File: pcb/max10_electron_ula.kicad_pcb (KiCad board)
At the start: 4 copper layers, 50 x 50 mm, 20 parts

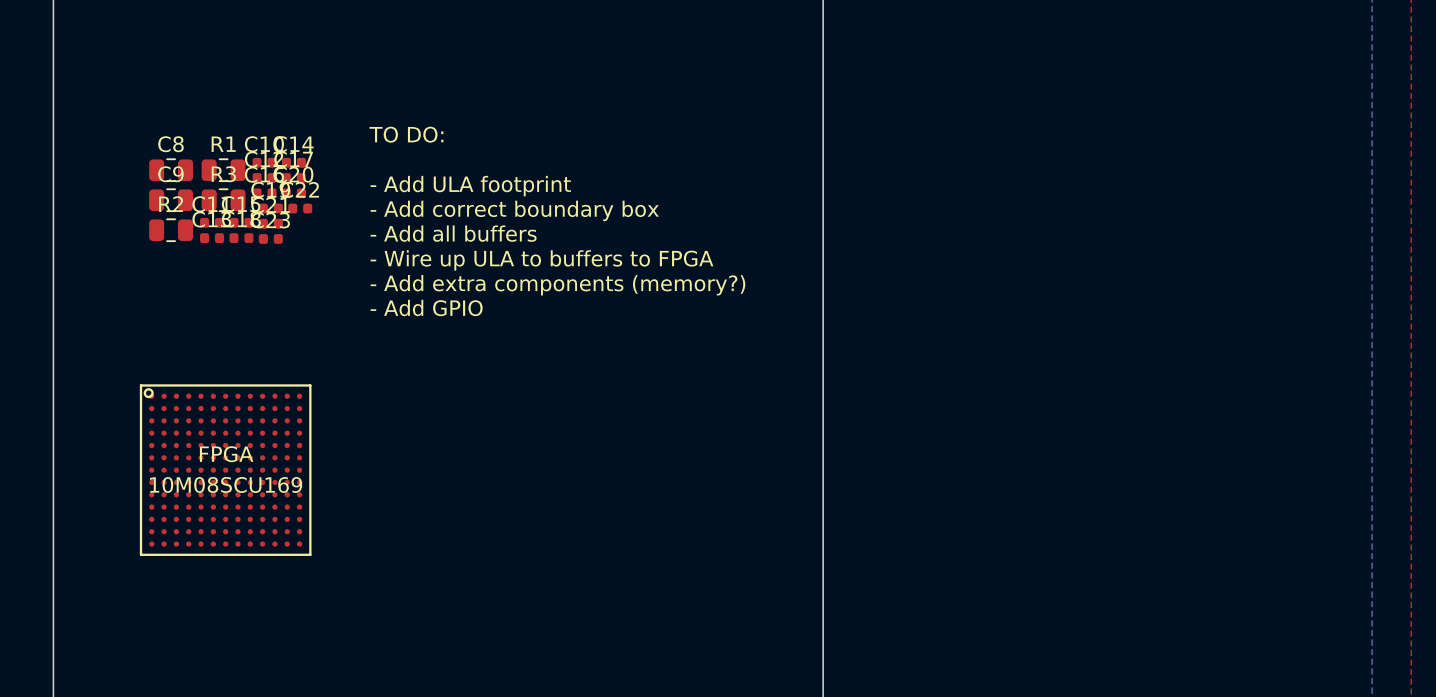
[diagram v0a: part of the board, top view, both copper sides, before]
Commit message: Added notes on ULA signals, with quotes from Stardot, and added ULA footprint
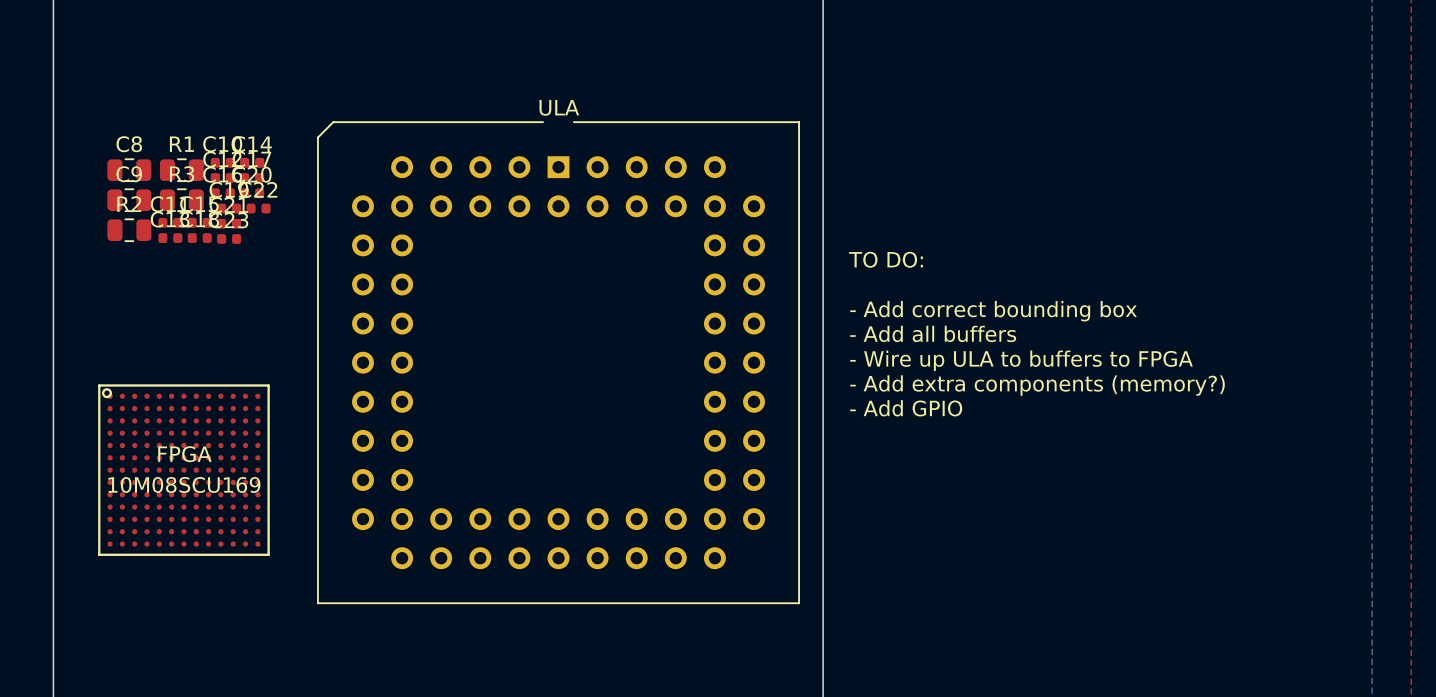
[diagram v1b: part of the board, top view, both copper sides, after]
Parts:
- added ULA: ULA header, Package_LCC:PLCC-68_THT-Socket, F.Cu at (147.8, 57.6)
- moved C10 2.71 mm to (126.0, 57.3)
- moved C11 2.71 mm to (122.6, 61.2)
- moved C12 2.71 mm to (126.0, 58.3)
- moved C13 2.71 mm to (122.6, 62.2)
- moved C15 2.71 mm to (124.5, 61.2)
- moved C16 2.71 mm to (126.0, 59.3)
- moved C18 2.71 mm to (124.5, 62.2)
- moved C22 2.71 mm to (128.3, 60.2)
- moved R1 2.71 mm to (123.3, 57.8)
- moved R3 2.71 mm to (123.3, 59.7)
- moved C14 2.71 mm to (127.9, 57.3)
- moved C17 2.71 mm to (127.9, 58.3)
- moved C19 2.71 mm to (126.4, 60.2)
- moved C20 2.71 mm to (127.9, 59.3)
- moved C21 2.71 mm to (126.4, 61.2)
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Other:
- board text added: "TO DO: - Add correct bounding box - Add all buffers - Wire up ULA to buffers to FPGA - Add extra components (memory?) - Add GPIO"
- board text removed: "TO DO: - Add ULA footprint - Add correct boundary box - Add all buffers - Wire up ULA to buffers to FPGA - Add extra components (memory?) - Add GPIO"

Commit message: Added 8MB flash chip
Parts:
- added FC0: 100n, Capacitor_SMD:C_0805_2012Metric_Pad1.15x1.40mm_HandSolder, F.Cu at (129.3, 85.3)
- added FC1: 100n, Capacitor_SMD:C_0805_2012Metric_Pad1.15x1.40mm_HandSolder, F.Cu at (129.3, 87.2)
- added FC2: 100n, Capacitor_SMD:C_0805_2012Metric_Pad1.15x1.40mm_HandSolder, F.Cu at (129.3, 89.2)
- added FLASH: S29GL064S70DHI010, myelin-kicad:cypress_lae064_fbga, F.Cu at (122.8, 88.9)

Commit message: Added 3.3V regulator and capacitors
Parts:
- added C1: 10u, Capacitor_SMD:C_0805_2012Metric_Pad1.15x1.40mm_HandSolder, F.Cu at (151.2, 68.4)
- added C2: 1u, Capacitor_SMD:C_0805_2012Metric_Pad1.15x1.40mm_HandSolder, F.Cu at (151.2, 70.3)
- added C3: 1u, Capacitor_SMD:C_0805_2012Metric_Pad1.15x1.40mm_HandSolder, F.Cu at (151.2, 72.3)
- added REG: AP7365-33YG-XX, Package_TO_SOT_SMD:SOT-89-3, F.Cu at (146.0, 70.0)
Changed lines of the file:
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@@
     (tracks 0)
     (zones 0)
-    (modules 25)
-    (nets 141)
+    (modules 29)
+    (nets 142)
   )
   (page A4)
@@
   (net 139 flash_DQ4)
   (net 140 flash_DQ6)
+  (net 141 5V)
   (net_class Default "This is the default net class."
     (clearance 0.127)
@@
     (uvia_dia 0.8128)
     (uvia_drill 0.3302)
+    (add_net 5V)
     (add_net C1_1)
     (add_net C1_10)
@@
       (solder_mask_margin 0.075) (clearance 0.1639))
   )
+  (module Capacitor_SMD:C_0805_2012Metric_Pad1.15x1.40mm_HandSolder (layer F.Cu)
+    (at 151.155001 68.375001)
+    (descr "Capacitor SMD 0805 (2012 Metric), square (rectangular) end terminal, IPC_7351 nominal with elongated pad for handsoldering. (Body size source: https://docs.google.com/spreadsheets/d/1BsfQQcO9C6DZCsRaXUlFlo91Tg2WpOkGARC1WS5S8t0/edit?usp=sharing), generated with kicad-footprint-generator")
+    (tags "capacitor handsolder")
+    (attr smd)
+    (fp_text reference C1 (at 0 -1.65) (layer F.SilkS)
+      (effects (font (size 1 1) (thickness 0.15)))
+    )
+    (fp_text value 10u (at 0 1.65) (layer F.Fab)
+      (effects (font (size 1 1) (thickness 0.15)))
+    )
+    (fp_line (start -1 0.6) (end -1 -0.6) (layer F.Fab) (width 0.1))
+    (fp_line (start -1 -0.6) (end 1 -0.6) (layer F.Fab) (width 0.1))
+    (fp_line (start 1 -0.6) (end 1 0.6) (layer F.Fab) (width 0.1))
+    (fp_line (start 1 0.6) (end -1 0.6) (layer F.Fab) (width 0.1))
+    (fp_line (start -0.261252 -0.71) (end 0.261252 -0.71) (layer F.SilkS) (width 0.12))
+    (fp_line (start -0.261252 0.71) (end 0.261252 0.71) (layer F.SilkS) (width 0.12))
+    (fp_line (start -1.85 0.95) (end -1.85 -0.95) (layer F.CrtYd) (width 0.05))
+    (fp_line (start -1.85 -0.95) (end 1.85 -0.95) (layer F.CrtYd) (width 0.05))
+    (fp_line (start 1.85 -0.95) (end 1.85 0.95) (layer F.CrtYd) (width 0.05))
+    (fp_line (start 1.85 0.95) (end -1.85 0.95) (layer F.CrtYd) (width 0.05))
+    (fp_text user %R (at 0 0) (layer F.Fab)
+      (effects (font (size 0.5 0.5) (thickness 0.08)))
+    )
+    (pad 1 smd roundrect (at -1.025 0) (size 1.15 1.4) (layers F.Cu F.Paste F.Mask) (roundrect_rratio 0.217391)
+      (net 2 GND))
+    (pad 2 smd roundrect (at 1.025 0) (size 1.15 1.4) (layers F.Cu F.Paste F.Mask) (roundrect_rratio 0.217391)
+      (net 141 5V))
+    (model ${KISYS3DMOD}/Capacitor_SMD.3dshapes/C_0805_2012Metric.wrl
+      (at (xyz 0 0 0))
+      (scale (xyz 1 1 1))
+      (rotate (xyz 0 0 0))
+    )
+  )
+  (module Capacitor_SMD:C_0805_2012Metric_Pad1.15x1.40mm_HandSolder (layer F.Cu)
+    (at 151.155001 70.325001)
+    (descr "Capacitor SMD 0805 (2012 Metric), square (rectangular) end terminal, IPC_7351 nominal with elongated pad for handsoldering. (Body size source: https://docs.google.com/spreadsheets/d/1BsfQQcO9C6DZCsRaXUlFlo91Tg2WpOkGARC1WS5S8t0/edit?usp=sharing), generated with kicad-footprint-generator")
+    (tags "capacitor handsolder")
+    (attr smd)
+    (fp_text reference C2 (at 0 -1.65) (layer F.SilkS)
+      (effects (font (size 1 1) (thickness 0.15)))
+    )
+    (fp_text value 1u (at 0 1.65) (layer F.Fab)
+      (effects (font (size 1 1) (thickness 0.15)))
+    )
+    (fp_text user %R (at 0 0) (layer F.Fab)
+      (effects (font (size 0.5 0.5) (thickness 0.08)))
+    )
+    (fp_line (start 1.85 0.95) (end -1.85 0.95) (layer F.CrtYd) (width 0.05))
+    (fp_line (start 1.85 -0.95) (end 1.85 0.95) (layer F.CrtYd) (width 0.05))
+    (fp_line (start -1.85 -0.95) (end 1.85 -0.95) (layer F.CrtYd) (width 0.05))
+    (fp_line (start -1.85 0.95) (end -1.85 -0.95) (layer F.CrtYd) (width 0.05))
+    (fp_line (start -0.261252 0.71) (end 0.261252 0.71) (layer F.SilkS) (width 0.12))
+    (fp_line (start -0.261252 -0.71) (end 0.261252 -0.71) (layer F.SilkS) (width 0.12))
+    (fp_line (start 1 0.6) (end -1 0.6) (layer F.Fab) (width 0.1))
+    (fp_line (start 1 -0.6) (end 1 0.6) (layer F.Fab) (width 0.1))
+    (fp_line (start -1 -0.6) (end 1 -0.6) (layer F.Fab) (width 0.1))
+    (fp_line (start -1 0.6) (end -1 -0.6) (layer F.Fab) (width 0.1))
+    (pad 2 smd roundrect (at 1.025 0) (size 1.15 1.4) (layers F.Cu F.Paste F.Mask) (roundrect_rratio 0.217391)
+      (net 141 5V))
+    (pad 1 smd roundrect (at -1.025 0) (size 1.15 1.4) (layers F.Cu F.Paste F.Mask) (roundrect_rratio 0.217391)
+      (net 2 GND))
+    (model ${KISYS3DMOD}/Capacitor_SMD.3dshapes/C_0805_2012Metric.wrl
+      (at (xyz 0 0 0))
+      (scale (xyz 1 1 1))
+      (rotate (xyz 0 0 0))
+    )
+  )
+  (module Capacitor_SMD:C_0805_2012Metric_Pad1.15x1.40mm_HandSolder (layer F.Cu)
+    (at 151.155001 72.275001)
+    (descr "Capacitor SMD 0805 (2012 Metric), square (rectangular) end terminal, IPC_7351 nominal with elongated pad for handsoldering. (Body size source: https://docs.google.com/spreadsheets/d/1BsfQQcO9C6DZCsRaXUlFlo91Tg2WpOkGARC1WS5S8t0/edit?usp=sharing), generated with kicad-footprint-generator")
+    (tags "capacitor handsolder")
+    (attr smd)
+    (fp_text reference C3 (at 0 -1.65) (layer F.SilkS)
+      (effects (font (size 1 1) (thickness 0.15)))
+    )
+    (fp_text value 1u (at 0 1.65) (layer F.Fab)
+      (effects (font (size 1 1) (thickness 0.15)))
+    )
+    (fp_line (start -1 0.6) (end -1 -0.6) (layer F.Fab) (width 0.1))
+    (fp_line (start -1 -0.6) (end 1 -0.6) (layer F.Fab) (width 0.1))
+    (fp_line (start 1 -0.6) (end 1 0.6) (layer F.Fab) (width 0.1))
+    (fp_line (start 1 0.6) (end -1 0.6) (layer F.Fab) (width 0.1))
+    (fp_line (start -0.261252 -0.71) (end 0.261252 -0.71) (layer F.SilkS) (width 0.12))
+    (fp_line (start -0.261252 0.71) (end 0.261252 0.71) (layer F.SilkS) (width 0.12))
+    (fp_line (start -1.85 0.95) (end -1.85 -0.95) (layer F.CrtYd) (width 0.05))
+    (fp_line (start -1.85 -0.95) (end 1.85 -0.95) (layer F.CrtYd) (width 0.05))
+    (fp_line (start 1.85 -0.95) (end 1.85 0.95) (layer F.CrtYd) (width 0.05))
+    (fp_line (start 1.85 0.95) (end -1.85 0.95) (layer F.CrtYd) (width 0.05))
+    (fp_text user %R (at 0 0) (layer F.Fab)
+      (effects (font (size 0.5 0.5) (thickness 0.08)))
+    )
+    (pad 1 smd roundrect (at -1.025 0) (size 1.15 1.4) (layers F.Cu F.Paste F.Mask) (roundrect_rratio 0.217391)
+      (net 1 3V3))
+    (pad 2 smd roundrect (at 1.025 0) (size 1.15 1.4) (layers F.Cu F.Paste F.Mask) (roundrect_rratio 0.217391)
+      (net 2 GND))
+    (model ${KISYS3DMOD}/Capacitor_SMD.3dshapes/C_0805_2012Metric.wrl
+      (at (xyz 0 0 0))
+      (scale (xyz 1 1 1))
+      (rotate (xyz 0 0 0))
+    )
+  )
+  (module Package_TO_SOT_SMD:SOT-89-3 (layer F.Cu)
+    (at 146.025001 69.975001)
+    (descr SOT-89-3)
+    (tags SOT-89-3)
+    (attr smd)
+    (fp_text reference REG (at 0.45 -3.2) (layer F.SilkS)
+      (effects (font (size 1 1) (thickness 0.15)))
+    )
+    (fp_text value AP7365-33YG-XX (at 0.45 3.25) (layer F.Fab)
+      (effects (font (size 1 1) (thickness 0.15)))
+    )
+    (fp_text user %R (at 0.38 0 90) (layer F.Fab)
+      (effects (font (size 0.6 0.6) (thickness 0.09)))
+    )
+    (fp_line (start 1.78 1.2) (end 1.78 2.4) (layer F.SilkS) (width 0.12))
+    (fp_line (start 1.78 2.4) (end -0.92 2.4) (layer F.SilkS) (width 0.12))
+    (fp_line (start -2.22 -2.4) (end 1.78 -2.4) (layer F.SilkS) (width 0.12))
+    (fp_line (start 1.78 -2.4) (end 1.78 -1.2) (layer F.SilkS) (width 0.12))
+    (fp_line (start -0.92 -1.51) (end -0.13 -2.3) (layer F.Fab) (width 0.1))
+    (fp_line (start 1.68 -2.3) (end 1.68 2.3) (layer F.Fab) (width 0.1))
+    (fp_line (start 1.68 2.3) (end -0.92 2.3) (layer F.Fab) (width 0.1))
+    (fp_line (start -0.92 2.3) (end -0.92 -1.51) (layer F.Fab) (width 0.1))
+    (fp_line (start -0.13 -2.3) (end 1.68 -2.3) (layer F.Fab) (width 0.1))
+    (fp_line (start 3.23 -2.55) (end 3.23 2.55) (layer F.CrtYd) (width 0.05))
+    (fp_line (start 3.23 -2.55) (end -2.48 -2.55) (layer F.CrtYd) (width 0.05))
+    (fp_line (start -2.48 2.55) (end 3.23 2.55) (layer F.CrtYd) (width 0.05))
+    (fp_line (start -2.48 2.55) (end -2.48 -2.55) (layer F.CrtYd) (width 0.05))
+    (pad 2 smd trapezoid (at 2.667 0 270) (size 1.6 0.85) (rect_delta 0 0.6 ) (layers F.Cu F.Paste F.Mask)
+      (net 2 GND))
+    (pad 1 smd rect (at -1.48 -1.5 270) (size 1 1.5) (layers F.Cu F.Paste F.Mask)
+      (net 1 3V3))
+    (pad 2 smd rect (at -1.3335 0 270) (size 1 1.8) (layers F.Cu F.Paste F.Mask)
+      (net 2 GND))
+    (pad 3 smd rect (at -1.48 1.5 270) (size 1 1.5) (layers F.Cu F.Paste F.Mask)
+      (net 141 5V))
+    (pad 2 smd rect (at 1.3335 0 270) (size 2.2 1.84) (layers F.Cu F.Paste F.Mask)
+      (net 2 GND))
+    (pad 2 smd trapezoid (at -0.0762 0 90) (size 1.5 1) (rect_delta 0 0.7 ) (layers F.Cu F.Paste F.Mask)
+      (net 2 GND))
+    (model ${KISYS3DMOD}/Package_TO_SOT_SMD.3dshapes/SOT-89-3.wrl
+      (at (xyz 0 0 0))
+      (scale (xyz 1 1 1))
+      (rotate (xyz 0 0 0))
+    )
+  )
   (gr_line (start 115 95) (end 115 45) (layer Edge.Cuts) (width 0.1))

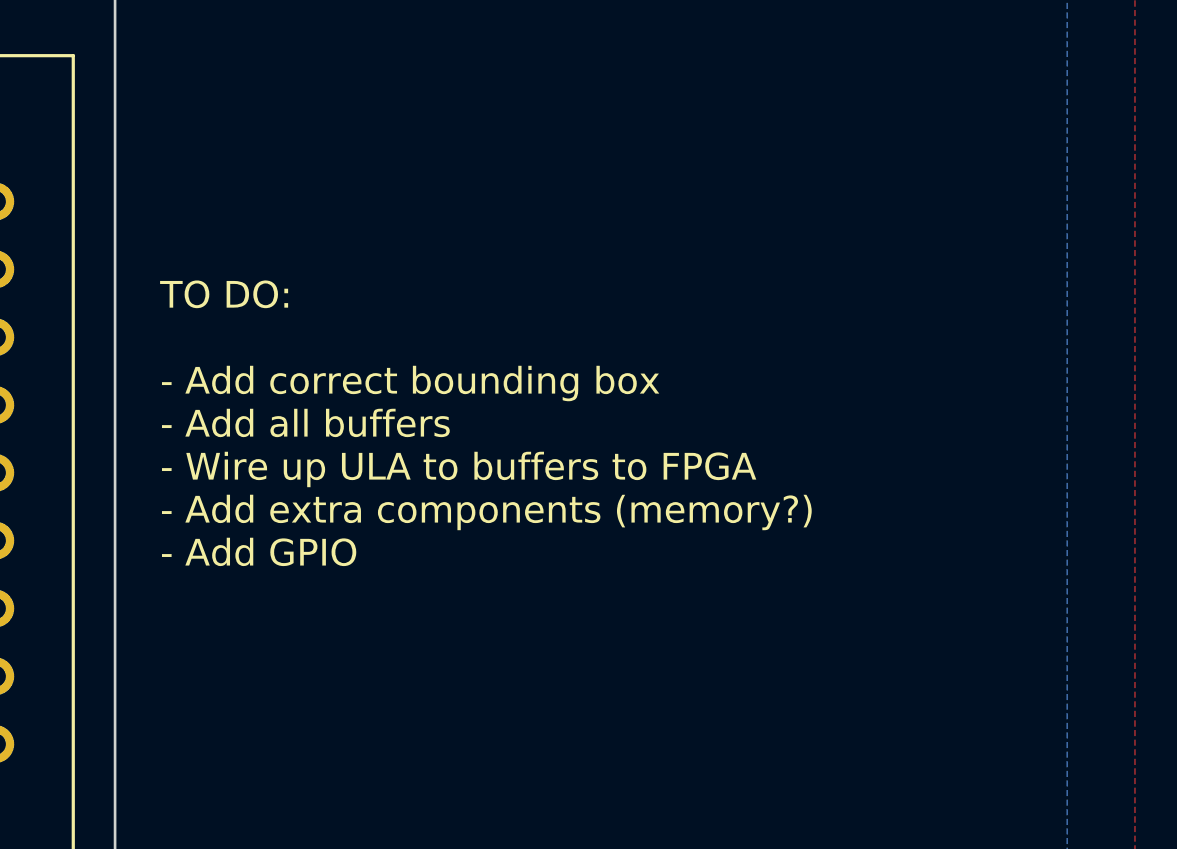
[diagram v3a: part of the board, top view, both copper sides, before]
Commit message: Added all ULA signals, and some RAM notes
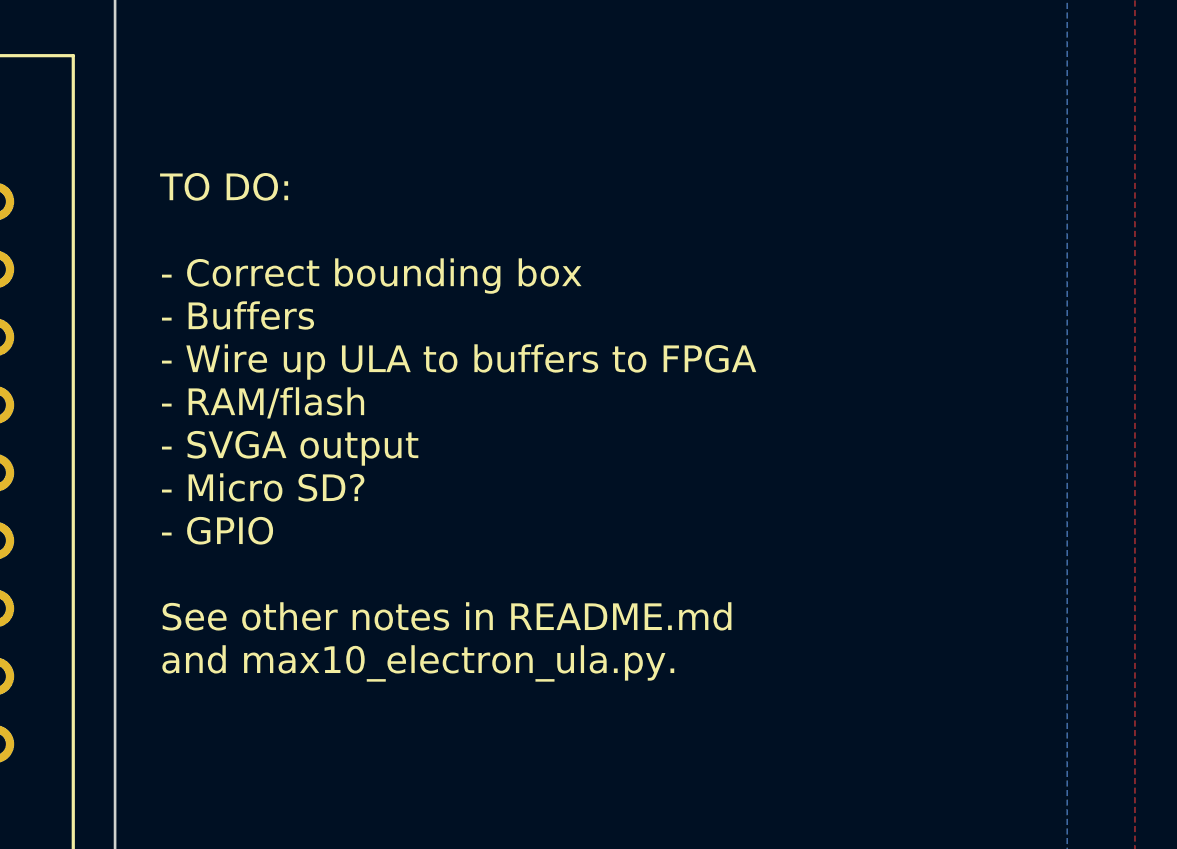
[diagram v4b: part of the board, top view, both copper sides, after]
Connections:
- ULA pad 1: (no net) -> A1_5V
- ULA pad 10: (no net) -> A14_5V
- ULA pad 11: (no net) -> 3V3
- ULA pad 12: (no net) -> A2_5V
- ULA pad 13: (no net) -> A12_5V
- ULA pad 14: (no net) -> A13_5V
- ULA pad 15: (no net) -> A7_5V
- ULA pad 16: (no net) -> 3V3
- ULA pad 17: (no net) -> A6_5V
- ULA pad 18: (no net) -> 3V3
- ULA pad 19: (no net) -> 3V3
- ULA pad 2: (no net) -> A8_5V
- ULA pad 20: (no net) -> A5_5V
- ULA pad 21: (no net) -> A4_5V
- ULA pad 22: (no net) -> 3V3
- ULA pad 23: (no net) -> A11_5V
- ULA pad 24: (no net) -> A3_5V
- ULA pad 25: (no net) -> A10_5V
- ULA pad 26: (no net) -> A9_5V
- ULA pad 27: (no net) -> KBD0_5V
- ULA pad 28: (no net) -> KBD1_5V
- ULA pad 29: (no net) -> 3V3
- ULA pad 3: (no net) -> RED_5V
- ULA pad 30: (no net) -> nIRQ_5V
- ULA pad 31: (no net) -> KBD2_5V
- ULA pad 32: (no net) -> KBD3_5V
- ULA pad 33: (no net) -> PD0_5V
- ULA pad 35: (no net) -> PD1_5V
- ULA pad 36: (no net) -> PD2_5V
- ULA pad 38: (no net) -> PD3_5V
- ULA pad 39: (no net) -> PD4_5V
- ULA pad 4: (no net) -> GREEN_5V
- ULA pad 41: (no net) -> PD5_5V
- ULA pad 42: (no net) -> PD6_5V
- ULA pad 43: (no net) -> 5V
- ULA pad 45: (no net) -> PD7_5V
- ULA pad 46: (no net) -> RnW_5V
- ULA pad 47: (no net) -> CAS_RC_5V
- ULA pad 48: (no net) -> 5V
- ULA pad 49: (no net) -> CLK_16MHZ_5V
- ULA pad 5: (no net) -> A0_5V
- ULA pad 50: (no net) -> CAS_OUT_5V
- ULA pad 51: (no net) -> GND
- ULA pad 52: (no net) -> 3V3
- ULA pad 53: (no net) -> 3V3
- ULA pad 54: (no net) -> nPOR_5V
- ULA pad 55: (no net) -> CLK_DIV13_5V
- ULA pad 56: (no net) -> A15_5V
- ULA pad 57: (no net) -> nNMI_5V
- ULA pad 58: (no net) -> nRESET
- ULA pad 59: (no net) -> CAS_IN_5V
- ULA pad 6: (no net) -> 3V3
- ULA pad 60: (no net) -> PHI_OUT_5V
- ULA pad 61: (no net) -> nROM
- ULA pad 62: (no net) -> SOUND_OUT_5V
- ULA pad 63: (no net) -> CAPS_LOCK
- ULA pad 64: (no net) -> CAS_MO_5V
- ULA pad 65: (no net) -> nCSYNC_5V
- ULA pad 66: (no net) -> BLUE_5V
- ULA pad 67: (no net) -> nHS_5V
- ULA pad 68: (no net) -> GND
- ULA pad 7: (no net) -> 3V3
- ULA pad 8: (no net) -> 3V3
- ULA pad 9: (no net) -> 5V
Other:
- board text added: "TO DO: - Correct bounding box - Buffers - Wire up ULA to buffers to FPGA - RAM/flash - SVGA output - Micro SD? - GPIO See other notes in README.md and max10_electron_ula.py."
- board text removed: "TO DO: - Add correct bounding box - Add all buffers - Wire up ULA to buffers to FPGA - Add extra components (memory?) - Add GPIO"

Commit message: Added SDRAM, and notes on serial flash
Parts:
- added RAM: MT48LC16M16A2, myelin-kicad:sdram_54tfbga, F.Cu at (140.6, 89.3)
- added REF**: SOIJ-8_5.3x5.3mm_P1.27mm, Package_SO:SOIJ-8_5.3x5.3mm_P1.27mm, F.Cu at (132.0, 103.1)
- added REF**: SOIC-8_3.9x4.9mm_P1.27mm, Package_SO:SOIC-8_3.9x4.9mm_P1.27mm, F.Cu at (158.3, 103.4)
- added REF**: hirose_micro_sd_card_socket, myelin-kicad:hirose_micro_sd_card_socket, F.Cu at (180.4, 89.9)
- moved ULA 3.68 mm to (147.9, 53.9)
